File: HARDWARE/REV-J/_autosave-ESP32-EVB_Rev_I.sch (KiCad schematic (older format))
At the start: 154 parts, among them CON1 TB3 DG306-5.0-3P, CON2 TB3 DG306-5.0-3P, Q1 BC817-40(SOT23), Q2 BC817-40(SOT23), Q3 Q12MHz/20pF/30ppm/2P/HC-49SM(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, Q4 BC817-40(SOT23), Q5 BC817-40(SOT23), Q6 BC817, Q7 BC817-40(SOT23), U1 BL4054B-42TPRN(SOT23-5), U10 BAT54C(SOT23-3), U2 SY8089AAAC(SOT23-5), U3 ESP-WROOM-32, U4 LAN8710A-EZC(QFN32), U5 CH340T(SSOP20W), U6 MCP2562-E/SN(SOIC-8_150mil), U7 RPM7236-H8, U8 NCP303LSN27T1G(SOT-23-5), U9 BAT54C(SOT23-3)

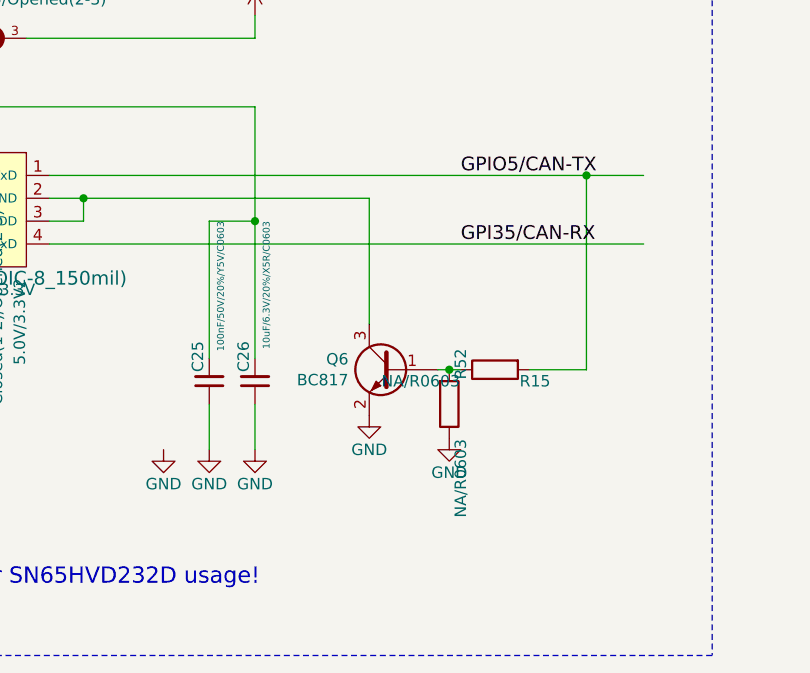
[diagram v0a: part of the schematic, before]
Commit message: fix auto control flow modbus
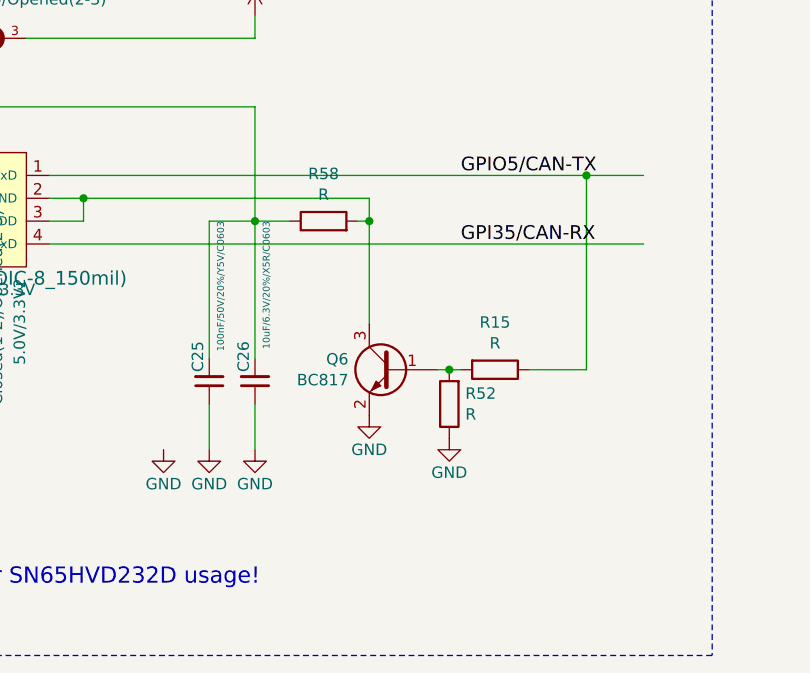
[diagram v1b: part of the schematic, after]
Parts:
- removed R15, R52: NA/R0603, OLIMEX_RLC-FP:R_0603_5MIL_DWS, symbol ESP32-EVB_Rev_I:R
- added R15, R52, R58: R, Resistor_SMD:R_0603_1608Metric, symbol Device:R
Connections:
- wire segments 697 -> 700
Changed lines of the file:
@@
 	13150 13800 14400 13800
 Wire Wire Line
-	14400 13800 14400 14350
+	14400 13800 14400 13900
 Connection ~ 13150 13800
 $Comp
@@
 	14700 14550 14750 14550
 $Comp
-L ESP32-EVB_Rev_I:R R52
-U 1 1 618069C7
+L Device:R R15
+U 1 1 614C248B
+P 14950 14550
+F 0 "R15" V 14743 14550 50  0000 C CNN
+F 1 "R" V 14834 14550 50  0000 C CNN
+F 2 "Resistor_SMD:R_0603_1608Metric" V 14880 14550 50  0001 C CNN
+F 3 "~" H 14950 14550 50  0001 C CNN
+	1    14950 14550
+	0    1    1    0
+$EndComp
+$Comp
+L Device:R R52
+U 1 1 614C4787
 P 14750 14700
-F 0 "R52" H 14925 14750 50  0000 C CNN
-F 1 "NA/R0603" H 14425 14750 50  0000 C CNN
-F 2 "OLIMEX_RLC-FP:R_0603_5MIL_DWS" V 14680 14700 30  0001 C CNN
-F 3 "" H 14750 14700 30  0000 C CNN
+F 0 "R52" H 14680 14654 50  0000 R CNN
+F 1 "R" H 14680 14745 50  0000 R CNN
+F 2 "Resistor_SMD:R_0603_1608Metric" V 14680 14700 50  0001 C CNN
+F 3 "~" H 14750 14700 50  0001 C CNN
 	1    14750 14700
-	0    1    -1   0
+	-1   0    0    1
 $EndComp
 Connection ~ 14750 14550
@@
 	14750 14550 14800 14550
 $Comp
-L ESP32-EVB_Rev_I:R R15
-U 1 1 618086CA
-P 14950 14550
-F 0 "R15" H 15125 14600 50  0000 C CNN
-F 1 "NA/R0603" H 14625 14600 50  0000 C CNN
-F 2 "OLIMEX_RLC-FP:R_0603_5MIL_DWS" V 14880 14550 30  0001 C CNN
-F 3 "" H 14950 14550 30  0000 C CNN
-	1    14950 14550
-	1    0    0    1
+L Device:R R58
+U 1 1 614C9259
+P 14200 13900
+F 0 "R58" V 14407 13900 50  0000 C CNN
+F 1 "R" V 14316 13900 50  0000 C CNN
+F 2 "Resistor_SMD:R_0603_1608Metric" V 14130 13900 50  0001 C CNN
+F 3 "~" H 14200 13900 50  0001 C CNN
+	1    14200 13900
+	0    -1   -1   0
 $EndComp
+Wire Wire Line
+	14050 13900 13900 13900
+Wire Wire Line
+	14350 13900 14400 13900
+Connection ~ 14400 13900
+Wire Wire Line
+	14400 13900 14400 14350
 $EndSCHEMATC

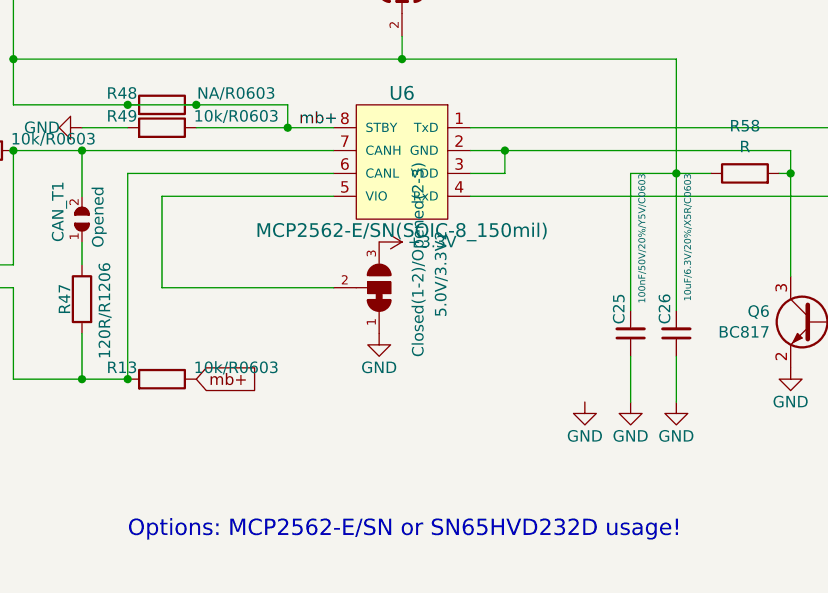
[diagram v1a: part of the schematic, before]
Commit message: done modbus 485
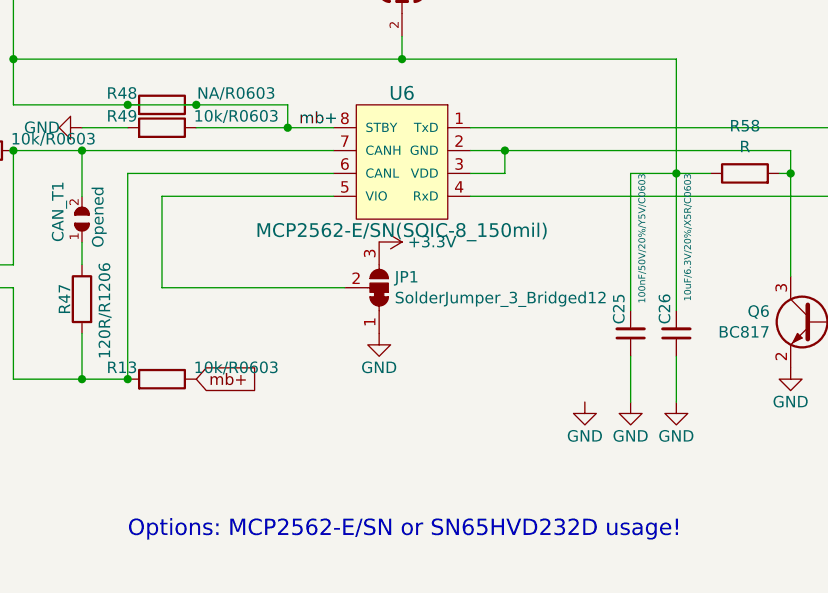
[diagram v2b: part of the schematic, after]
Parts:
- removed 5.0V/3.3V2: Closed(1-2)/Opened(2-3), OLIMEX_Jumpers-FP:SJ_2_SMALL_12_TIED, symbol ESP32-EVB_Rev_I:SJ2W_Closed(1-2)
- added JP1: SolderJumper_3_Bridged12, Jumper:SolderJumper-3_P1.3mm_Bridged2Bar12_Pad1.0x1.5mm_NumberLabels, symbol Jumper:SolderJumper_3_Bridged12
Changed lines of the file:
@@
-$EndComp
-$Comp
-L ESP32-EVB_Rev_I:SJ2W_Closed(1-2) 5.0V/3.3V2
-U 1 1 61B60BDC
-P 12600 14400
-F 0 "5.0V/3.3V2" V 12900 14150 50  0000 L BNN
-F 1 "Closed(1-2)/Opened(2-3)" V 12800 13850 50  0000 L BNN
-F 2 "OLIMEX_Jumpers-FP:SJ_2_SMALL_12_TIED" H 12630 14550 20  0001 C CNN
-F 3 "" H 12600 14400 60  0000 C CNN
-	1    12600 14400
-	1    0    0    1
 $EndComp
 $Comp
@@
 	1    0    0    -1
 $EndComp
-Wire Wire Line
-	12400 14400 11650 14400
 Wire Wire Line
 	11650 14400 11650 14000
@@
 Wire Wire Line
 	14400 13900 14400 14350
+$Comp
+L Jumper:SolderJumper_3_Bridged12 JP1
+U 1 1 616705BA
+P 12600 14400
+F 0 "JP1" V 12646 14468 50  0000 L CNN
+F 1 "SolderJumper_3_Bridged12" V 12555 14468 50  0000 L CNN
+F 2 "Jumper:SolderJumper-3_P1.3mm_Bridged2Bar12_Pad1.0x1.5mm_NumberLabels" H 12600 14400 50  0001 C CNN
+F 3 "~" H 12600 14400 50  0001 C CNN
+	1    12600 14400
+	0    1    -1   0
+$EndComp
+Wire Wire Line
+	11650 14400 12450 14400
 $EndSCHEMATC
